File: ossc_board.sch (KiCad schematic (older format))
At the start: 4 parts

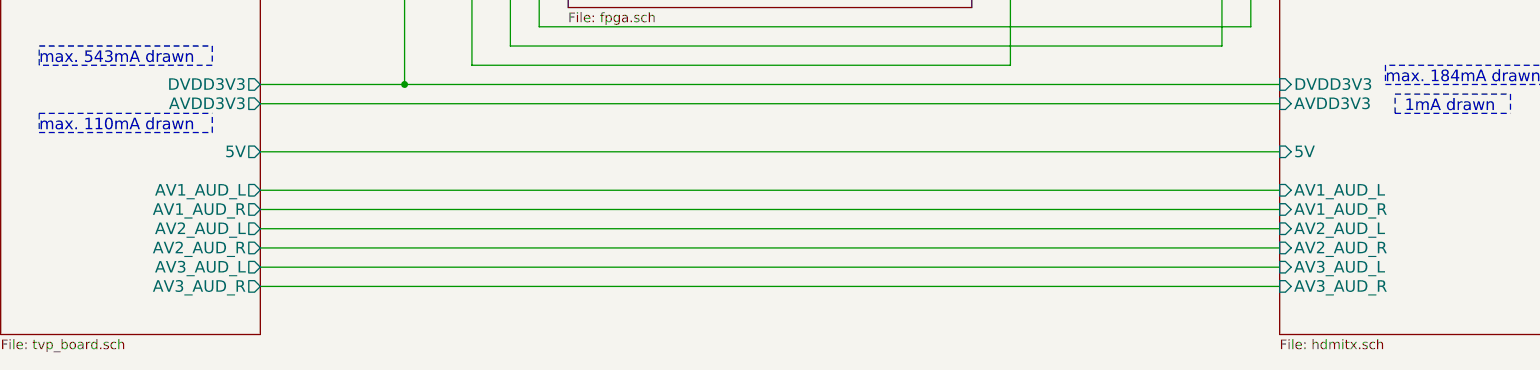
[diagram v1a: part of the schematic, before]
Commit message: remove unnecessary component
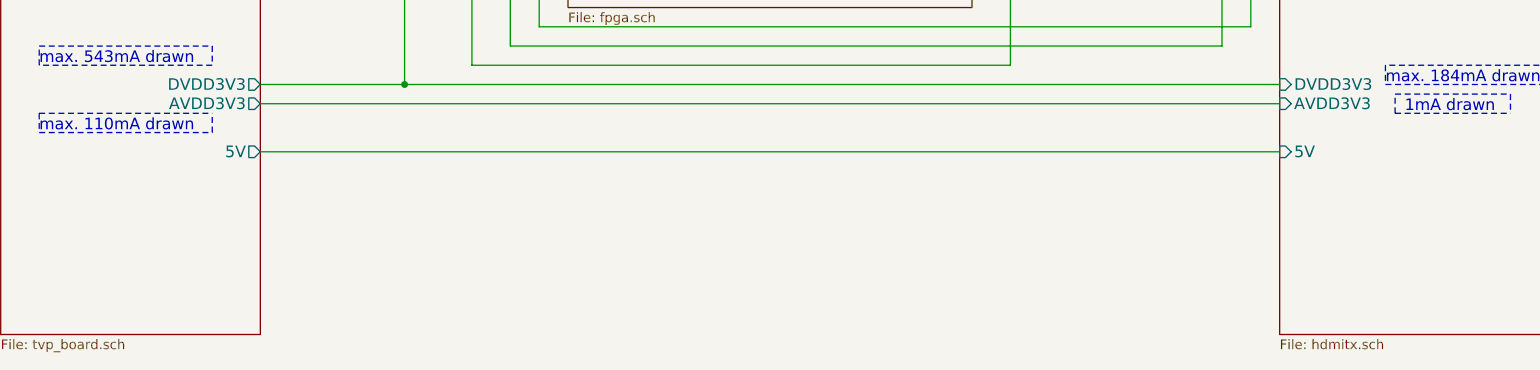
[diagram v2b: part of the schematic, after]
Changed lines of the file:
@@
 F35 "CLK27" O R 3050 4400 60
 F36 "5V" O R 3050 5900 60
-F37 "AV2_AUD_L" O R 3050 6300 60
-F38 "AV2_AUD_R" O R 3050 6400 60
-F39 "AV1_AUD_L" O R 3050 6100 60
-F40 "AV1_AUD_R" O R 3050 6200 60
-F41 "AV3_AUD_L" O R 3050 6500 60
-F42 "AV3_AUD_R" O R 3050 6600 60
 $EndSheet
 Text Notes 5050 4850 0    60   ~ 0
@@
 F35 "AVDD3V3" I L 8350 5650 60
 F36 "5V" I L 8350 5900 60
-F37 "AV1_AUD_L" I L 8350 6100 60
-F38 "AV1_AUD_R" I L 8350 6200 60
-F39 "AV2_AUD_L" I L 8350 6300 60
-F40 "AV2_AUD_R" I L 8350 6400 60
-F41 "AV3_AUD_L" I L 8350 6500 60
-F42 "AV3_AUD_R" I L 8350 6600 60
 $EndSheet
 $Comp
@@
 NoConn ~ 10400 6400
 Wire Wire Line
-	3050 6100 8350 6100
-Wire Wire Line
-	3050 6200 8350 6200
-Wire Wire Line
-	3050 6300 8350 6300
-Wire Wire Line
-	3050 6400 8350 6400
-Wire Wire Line
-	3050 6500 8350 6500
-Wire Wire Line
-	3050 6600 8350 6600
-Wire Wire Line
 	4500 4700 4650 4700

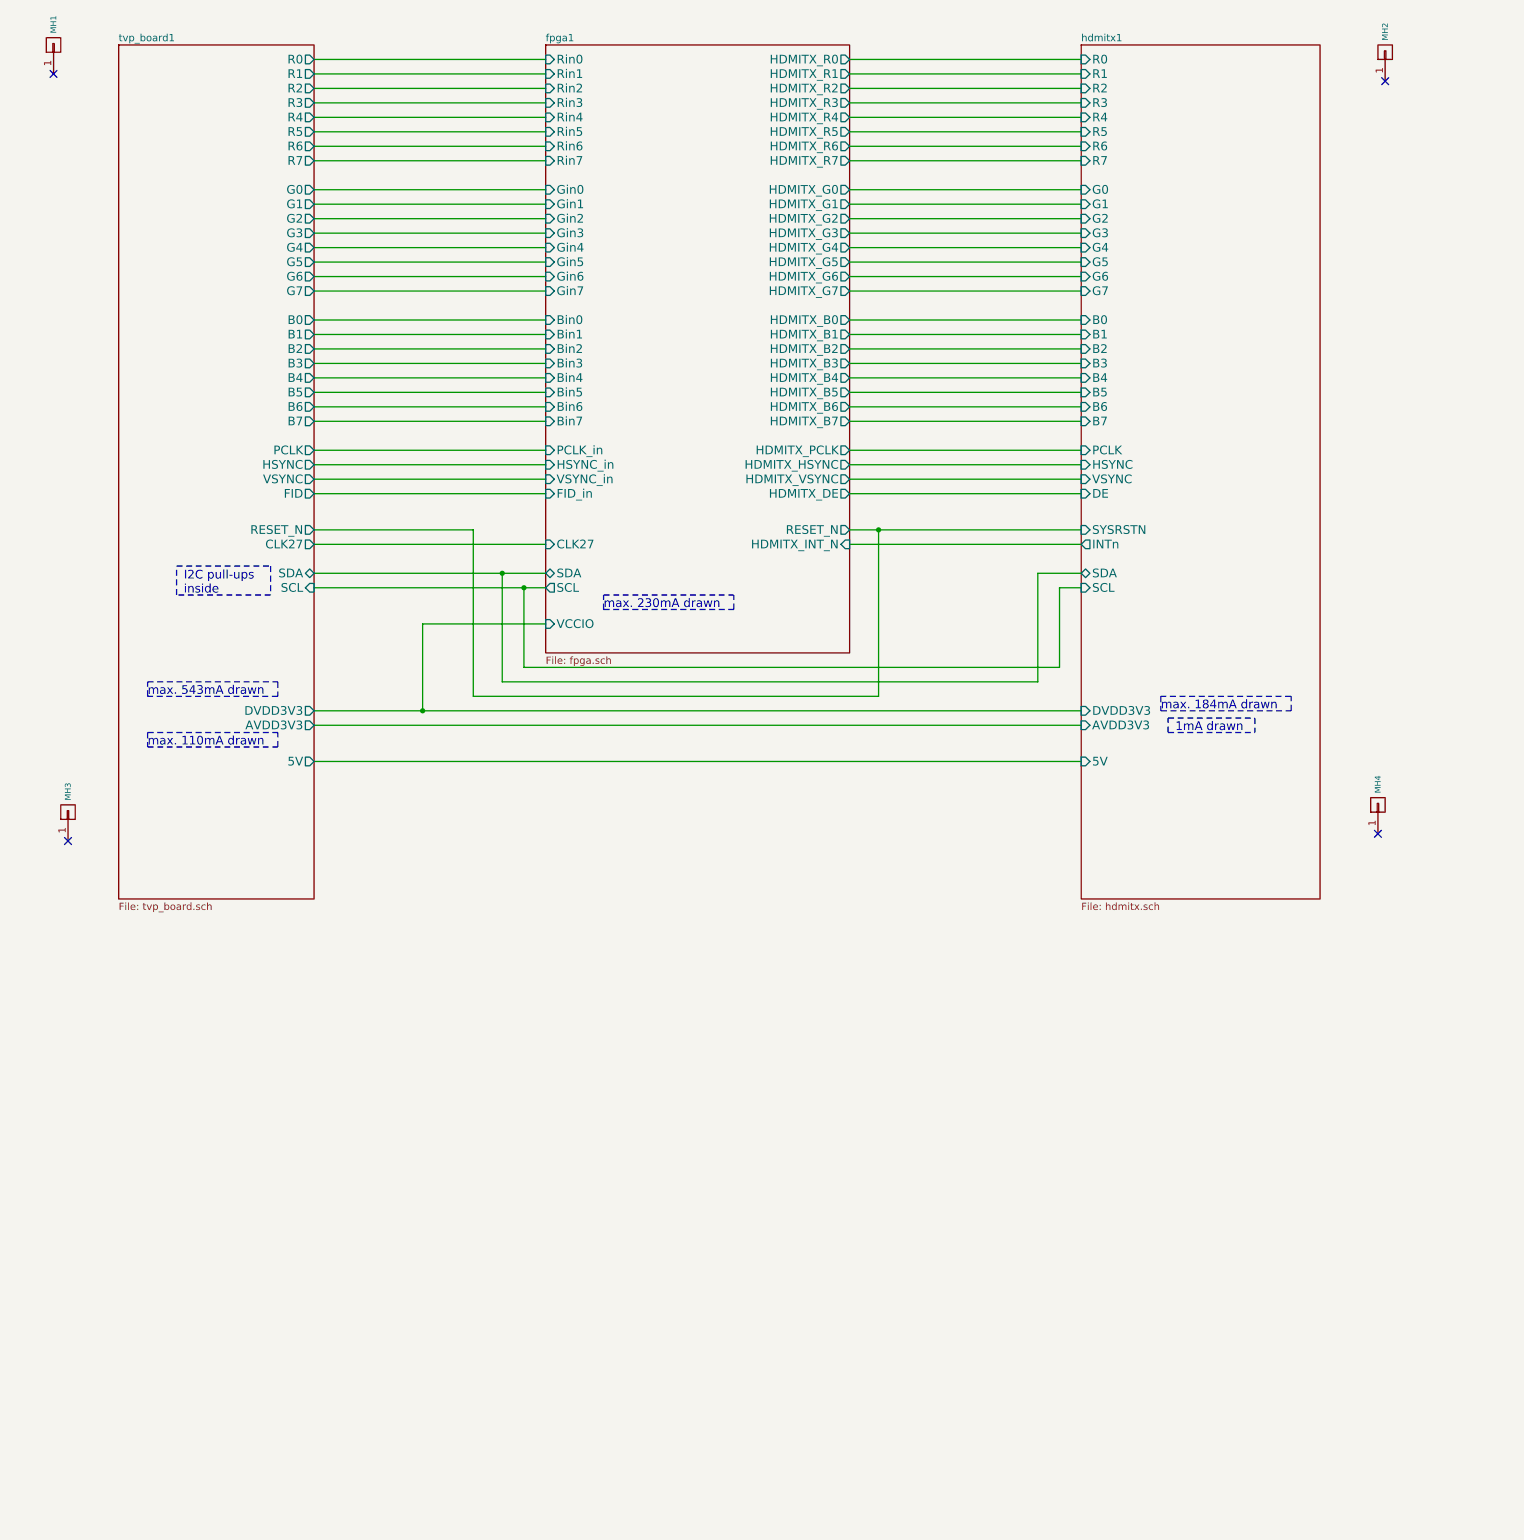
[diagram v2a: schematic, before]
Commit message: NeXT Sound Box function (1st rev) (#1)
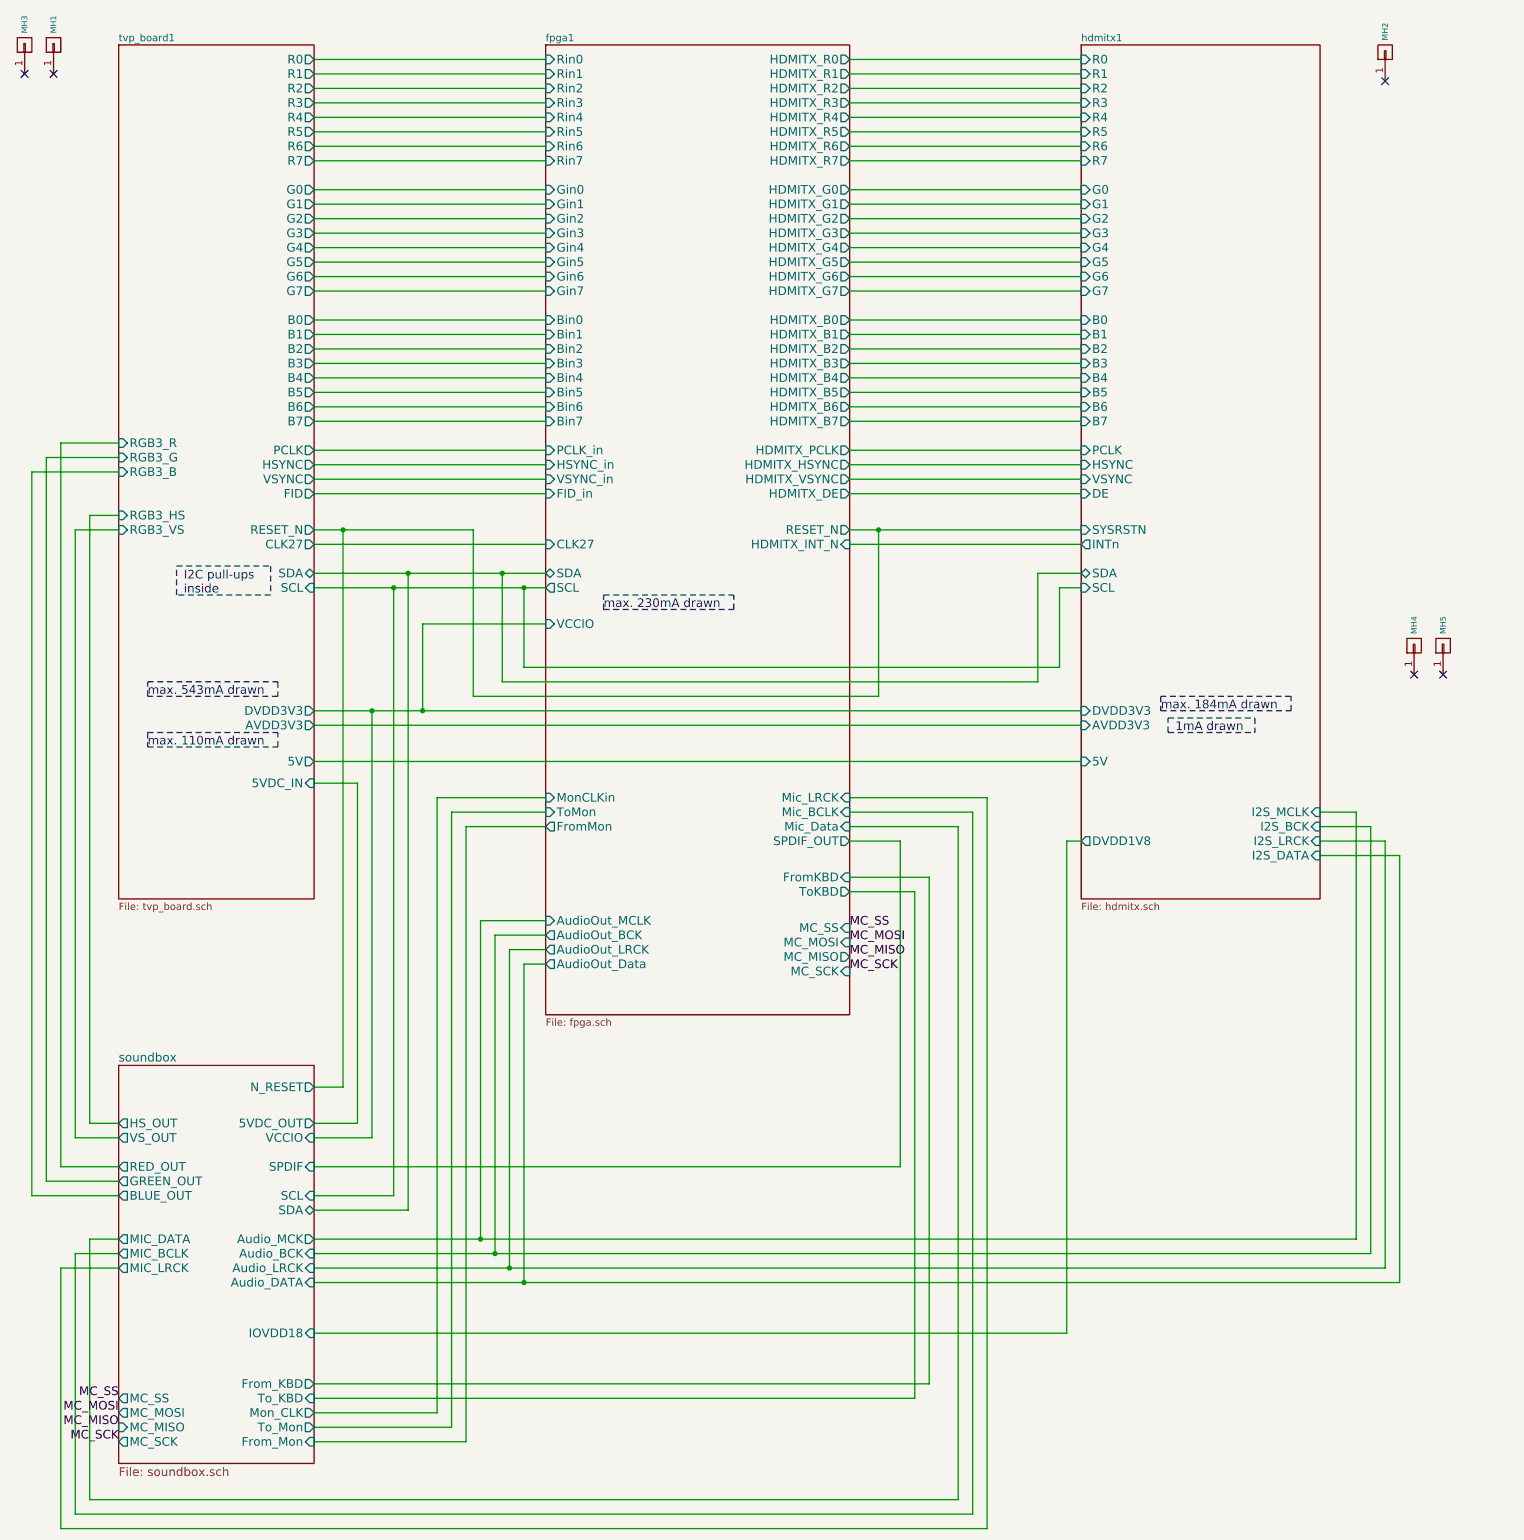
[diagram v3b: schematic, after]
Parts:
- added MH5: CONN_1, MountingHole:MountingHole_2.7mm_M2.5, symbol ossc_board-rescue:CONN_01X01
- MH1, MH2, MH3, MH4: footprint Connect:1pin -> MountingHole:MountingHole_2.7mm_M2.5
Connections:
- no-connect marks 4 -> 5
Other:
- moved on the sheet: MH3, MH4

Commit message: update
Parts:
- added MH6: TestHole1, custom_components:TestHole_1.0mm, symbol ossc_board-rescue:CONN_01X01
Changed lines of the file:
@@
 $EndComp
 NoConn ~ 10850 5300
+$Comp
+L ossc_board-rescue:CONN_01X01 MH6
+U 1 1 60C62675
+P 11200 5750
+F 0 "MH6" H 11280 5750 40  0000 L CNN
+F 1 "TestHole1" H 11250 5650 30  0000 C CNN
+F 2 "custom_components:TestHole_1.0mm" H 11200 5750 60  0001 C CNN
+F 3 "" H 11200 5750 60  0000 C CNN
+	1    11200 5750
+	0    -1   -1   0
+$EndComp
 $EndSCHEMATC

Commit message: update values
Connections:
- no-connect marks 5 -> 6
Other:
- moved on the sheet: MH6
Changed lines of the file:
@@
 L ossc_board-rescue:CONN_01X01 MH6
 U 1 1 60C62675
-P 11200 5750
-F 0 "MH6" H 11280 5750 40  0000 L CNN
-F 1 "TestHole1" H 11250 5650 30  0000 C CNN
-F 2 "custom_components:TestHole_1.0mm" H 11200 5750 60  0001 C CNN
-F 3 "" H 11200 5750 60  0000 C CNN
-	1    11200 5750
+P 11200 5100
+F 0 "MH6" H 11280 5100 40  0000 L CNN
+F 1 "TestHole1" H 11250 5000 30  0000 C CNN
+F 2 "custom_components:TestHole_1.0mm" H 11200 5100 60  0001 C CNN
+F 3 "" H 11200 5100 60  0000 C CNN
+	1    11200 5100
 	0    -1   -1   0
 $EndComp
+NoConn ~ 11200 5300
 $EndSCHEMATC
